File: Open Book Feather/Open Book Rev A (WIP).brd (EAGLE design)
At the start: 77.5 x 112.3 mm, 111 parts, among them J1 SJ-43514-SMT, J2 10118193-0001LF, Q1 DMG341, Q2 IRLML0100, SW1 SPDT_SWITCH, U1 AP2112-3.3, U2 MCP73831T-2ACI/OT, U3 ATSAMD51J64-TQFP(10X10), U4 GD25Q64, U5 74AC165D, U7 23K256-I/SN, X1 JSTPH, X2 2x5 0.05" SWD

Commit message: clarify flash chips
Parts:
- U4: value GD25Q64 -> GD25Q16C (or GD25Q32C)
- U6: value (none) -> GD25Q16C (or GD25Q32C)
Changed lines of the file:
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@@
 <layer number="27" name="tValues" color="7" fill="1" visible="no" active="yes"/>
 <layer number="28" name="bValues" color="7" fill="1" visible="no" active="yes"/>
-<layer number="29" name="tStop" color="7" fill="3" visible="yes" active="yes"/>
+<layer number="29" name="tStop" color="7" fill="3" visible="no" active="yes"/>
 <layer number="30" name="bStop" color="7" fill="6" visible="no" active="yes"/>
 <layer number="31" name="tCream" color="7" fill="4" visible="no" active="yes"/>
 <layer number="32" name="bCream" color="7" fill="5" visible="no" active="yes"/>
-<layer number="33" name="tFinish" color="6" fill="3" visible="yes" active="yes"/>
+<layer number="33" name="tFinish" color="6" fill="3" visible="no" active="yes"/>
 <layer number="34" name="bFinish" color="6" fill="6" visible="no" active="yes"/>
-<layer number="35" name="tGlue" color="7" fill="4" visible="yes" active="yes"/>
+<layer number="35" name="tGlue" color="7" fill="4" visible="no" active="yes"/>
 <layer number="36" name="bGlue" color="7" fill="5" visible="no" active="yes"/>
 <layer number="37" name="tTest" color="7" fill="1" visible="no" active="yes"/>
@@
 <layer number="127" name="_tValues" color="7" fill="1" visible="no" active="yes"/>
 <layer number="128" name="_bValues" color="7" fill="1" visible="no" active="yes"/>
-<layer number="129" name="Mask" color="7" fill="1" visible="yes" active="yes"/>
+<layer number="129" name="Mask" color="7" fill="1" visible="no" active="yes"/>
 <layer number="130" name="SMDSTROOK" color="7" fill="1" visible="no" active="yes"/>
 <layer number="131" name="tAdjust" color="7" fill="1" visible="no" active="yes"/>
@@
 <layer number="251" name="SMDround" color="12" fill="11" visible="no" active="no"/>
 <layer number="254" name="cooling" color="7" fill="1" visible="no" active="yes"/>
-<layer number="255" name="routoute" color="7" fill="1" visible="yes" active="yes"/>
+<layer number="255" name="routoute" color="7" fill="1" visible="no" active="yes"/>
 </layers>
 <board>
@@
 <attribute name="VALUE" x="29.972" y="111.76" size="0.508" layer="28" font="vector" ratio="18" rot="MR90" align="center"/>
 </element>
-<element name="U4" library="microbuilder" package="SOIC8_150MIL" value="GD25Q64" x="26.162" y="30.734" smashed="yes" rot="MR180">
+<element name="U4" library="microbuilder" package="SOIC8_150MIL" value="GD25Q16C (or GD25Q32C)" x="26.162" y="30.734" smashed="yes" rot="MR180">
 <attribute name="NAME" x="29.083" y="30.607" size="0.508" layer="26" font="vector" ratio="18" rot="MR90" align="center"/>
 <attribute name="VALUE" x="24.257" y="31.115" size="0.508" layer="28" font="vector" ratio="18" rot="MR180" align="center"/>
@@
 </element>
 <element name="U$23" library="My Stuff" package="OSO-TEXT-TEST" value="OSO-TEXT-TEST" x="62.23" y="123.698" smashed="yes" rot="MR0"/>
-<element name="U6" library="Adafruit Feather M0 Express" package="MICROBUILDER_SOIC8_150MIL" value="" x="53.34" y="30.734" smashed="yes" rot="MR180">
+<element name="U6" library="Adafruit Feather M0 Express" package="MICROBUILDER_SOIC8_150MIL" value="GD25Q16C (or GD25Q32C)" x="53.34" y="30.734" smashed="yes" rot="MR180">
 <attribute name="NAME" x="56.261" y="30.861" size="0.508" layer="26" font="vector" ratio="18" rot="MR90" align="center"/>
 <attribute name="VALUE" x="51.435" y="31.115" size="0.4064" layer="28" ratio="10" rot="MR180"/>

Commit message: add logos and such
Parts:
- added U$44: OSO_GRAPHIC, My Stuff:OSO_GRAPHIC
- added U$45: OSO_BEAR, My Stuff:OSO_BEAR_750MIL
- added U$47: OSO_TEXT, My Stuff:OSO_TEXT_435MIL
- added U$48: OSO_TEXTOSO_TEXT_ONELINE_125MIL, My Stuff:OSO_ONELINE_125MIL
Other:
- board text added: "*Notes on this bit can be found at end of the POWER SUPPLY block."
- board text added: "SAMD51 MICROCONTROLLER"
- board text added: "USB, BATTERY AND LOGO:"
- board text added: "Uses the main SPI bus (MISO, MOSI, SCK). Chip select is D4."
- board text added: "You can stash a small battery between the Feather headers!"
- board text removed: "BATTERY"
- board text removed: "Notes on this block @end of `POWER SUPPLY'"
- board text removed: "SAM D51 MICROCONTROLLER"
- board text removed: "Uses the main SPI bus (MISO, MOSI, SCK). Chip select is D4, v also over there."

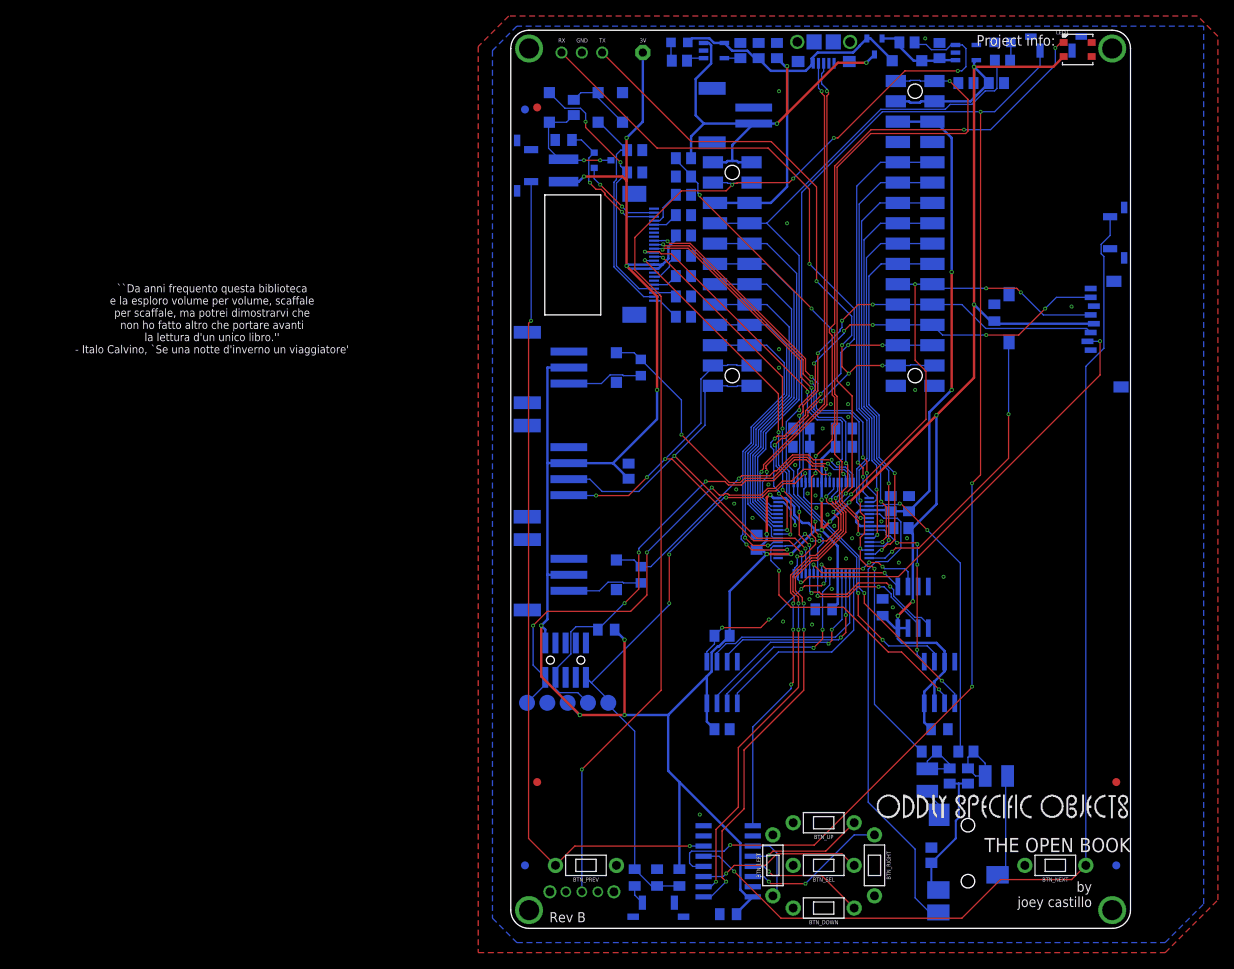
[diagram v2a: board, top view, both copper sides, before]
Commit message: move leds topside, thru-hole style. other design tweaks
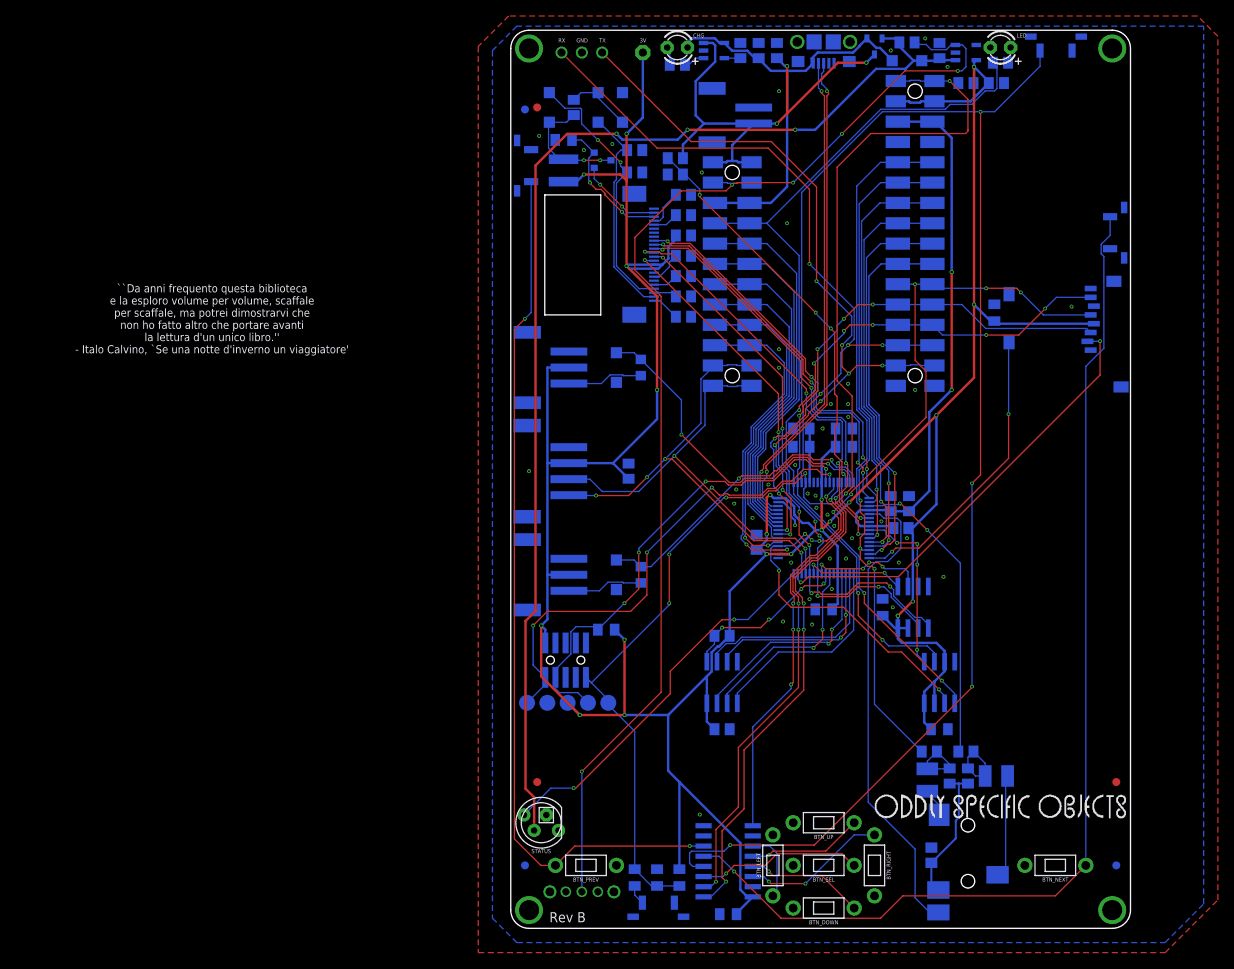
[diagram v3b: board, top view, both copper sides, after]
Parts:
- removed LED1: WS2812B3535, microbuilder:LED3535
- added STATUS: WS2812B, adafruit:LED5MMRGB
- CHG: value ORANGE -> AMBER; device microbuilder:CHIPLED_0805_NOOUTLINE -> adafruit:LED3MM
- LED: value RED -> RED OR GRN; device microbuilder:CHIPLED_0805_NOOUTLINE -> adafruit:LED3MM
- moved R14 1.05 mm to (20.3, 94.2)
- moved R15 1.02 mm to (20.3, 96.3)
- moved CHG 0.68 mm to (20.6, 110.1), flipped to the top, turned to 180 degrees
- moved LED 0.68 mm to (61.0, 110.1), flipped to the top, turned to 180 degrees
- moved R4 0.57 mm to (20.6, 108.0)
- moved R8 0.36 mm to (61.0, 108.2)
- moved U$48 0.25 mm to (45.2, 15.2)
- moved U$47 0.08 mm to (38.9, 78.8)
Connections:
- removed net VHI: C1.1, D1.C, Q1.2, R1.2, U1.1
- new net V+: C1.1, D1.C, Q1.2, R1.2, STATUS.3, U1.1
- net +3V3: no longer LED1.2
- net D8_NEOPIX: now also STATUS.4; no longer LED1.1
- net GND: now also LED.K, STATUS.2; no longer LED.C, LED1.4
- net N$4: now also CHG.K; no longer CHG.C
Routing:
- net V+: track 0.00 -> 148.3 mm, vias 0 -> 3
- net D8_NEOPIX: track 90.8 -> 47.8 mm, vias 5 -> 2
- net +3V3: track 461.1 -> 449.6 mm
- net VHI: track 10.9 -> 0.00 mm
- net BUTTON7: track 106.5 -> 109.0 mm
- net VBAT: track 60.4 -> 61.5 mm
- net VBUS: track 55.5 -> 56.1 mm
- net A6_VMEAS: track 49.6 -> 50.2 mm
- net GND: vias 37 -> 44
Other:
- board text added: "BABEL FLASH CHIP"
- board text added: "CREDIT: by Joey Castillo @josecastillo. Based in large part on Adafruit's open source designs. OSO Logo & lazer bear by Joseph Devens @DoctorDevens."
- board text added: "STATUS LED"
- board text added: "THANKS TO: Josh L, Tom F, Brent R"
- board text added: "The center port provides an I2C interface. The other two ports provide access to pins A8 and A9. D5 & D6 + R17 & R18 provide protection and current limiting."
- board text removed: "@josecastillo"
- board text removed: "ACKNOWLEDGMENTS By Joey Castillo / @josecastillo. Based heavily on @Adafruit's open source designs. OSO Logo and font by Joseph Devens @DoctorDevens."
- board text removed: "GNU UNIFONT FLASH"
- board text removed: "Project info:"
- board text removed: "The center port provides an I2C interface. The other two ports provide access to pins A1 and A2. D5 & D6 + R17 & R18 provide protection and current limiting."
- board text removed: "You can stash a small battery between the Feather headers!"
- board text removed: "github.com/joeycastillo/The-Open-Book"

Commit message: add these cool right-angle LEDs (that i ordered too many of)
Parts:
- CHG, LED: device adafruit:LED3MM -> adafruit:LED17X45_SIDEVIEW
- moved LED 0.68 mm to (61.2, 110.7), flipped to the bottom
- moved CHG 0.64 mm to (20.6, 110.7), flipped to the bottom
- moved JP1 0.64 mm to (8.64, 108.8)
- moved JP2 0.64 mm to (16.3, 108.8)
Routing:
- net VBUS: track 56.1 -> 58.4 mm
- net N$4: track 2.29 -> 3.71 mm
- net N$7: track 2.04 -> 3.35 mm
- net +3V3: track 449.6 -> 448.9 mm
